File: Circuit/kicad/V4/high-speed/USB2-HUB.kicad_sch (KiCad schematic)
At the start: 37 parts, among them J10 USB_C_Receptacle_USB2.0_16P, J7 690-008-221-904, J8 USB_C_Receptacle_USB2.0_16P, U10 TPD4EUSB30, U11 USB2514B-I/M2, U12 TPD4EUSB30, U13 FSUSB42MUX, U8 FSUSB42MUX, U9 AP22653W6, Y1 24MHz

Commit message: high speed first step
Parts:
- renumbered C13 to C15, C12 to C16, C14 to C17, C17 to C18, C18 to C19, C19 to C20, C20 to C21, C21 to C22, C15 to C23, C16 to C24, CT2 to CT3, J8 to J10, J10 to J11, J7 to J12, R23 to R15, R30 to R16, R24 to R17, R32 to R18, R17 to R19, R28 to R20, R16 to R21, R27 to R22, R18 to R23, R22 to R24, R19 to R25, R20 to R26, R21 to R27, R25 to R28, R26 to R29, TP9 to TP35, U13 to U10, U9 to U13, U10 to U9
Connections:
- net CH343P_usbD+ is gone; now on net ESP_usbD+: U10.3 (D_P)
- net CH343P_usbD- is gone; now on net ESP_usbD-: U10.4 (D_N)
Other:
- moved on the sheet: C18, C19, C20, C21, C22, C23, C24, CT3, J11, J12, R16, R18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

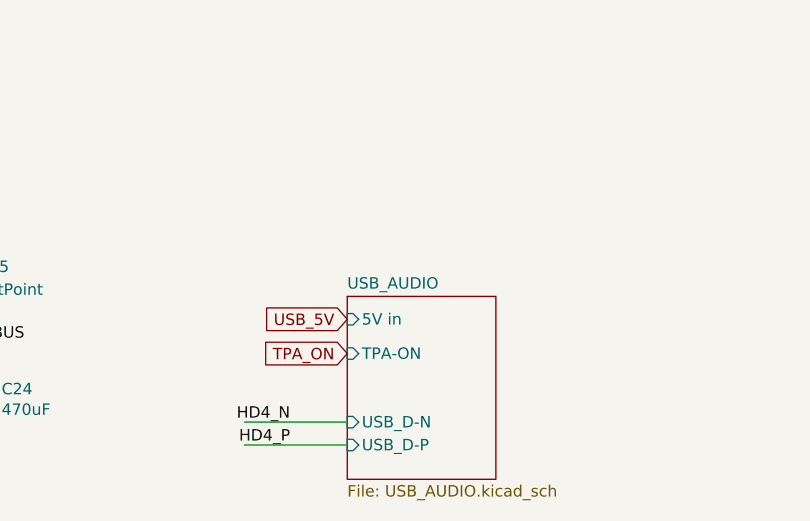
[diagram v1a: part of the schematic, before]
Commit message: added psu start delay rc tag, high speed first inner and outboard impedance calculations
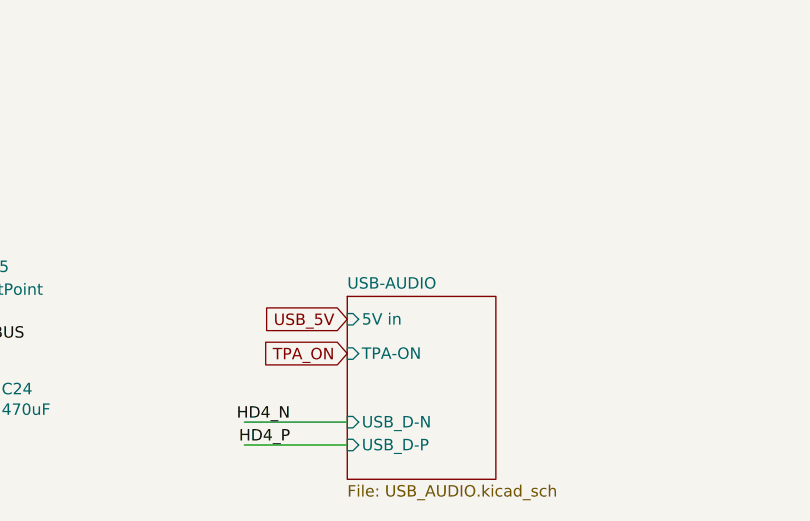
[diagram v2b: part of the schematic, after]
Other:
- sheet USB_AUDIO renamed USB-AUDIO
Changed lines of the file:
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@@
 			(color 0 0 0 0.0000)
 		)
-		(property "Sheetname" "USB_AUDIO"
+		(property "Sheetname" "USB-AUDIO"
 			(at 182.88 245.6684 0)
 			(effects

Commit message: kicad: high speed V2.2 Circuit finish psu bom update
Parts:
- C21: renamed from C15; Cikkszám (none) -> 100.011.22; Link (none) -> https://www.hestore.hu/prod_10001122.html
- C22: renamed from C16; Cikkszám (none) -> 100.011.31; Field4 Digikey -> (none); Field5 490-17672-1-ND -> (none); Field6 GJM1555C1H270JB01D -> (none); Field7 Murata -> (none); Field8 UCAP00738 -> (none); Link (none) -> https://www.hestore.hu/prod_10001131.html; Part Description 27pF 5% 50V Ceramic Capacitor C0G, NP0 0402 (1005 Metric) -> (none)
- C23: renamed from C17; Cikkszám (none) -> 100.011.31; Field4 Digikey -> (none); Field5 490-17672-1-ND -> (none); Field6 GJM1555C1H270JB01D -> (none); Field7 Murata -> (none); Field8 UCAP00738 -> (none); Link (none) -> https://www.hestore.hu/prod_10001131.html; Part Description 27pF 5% 50V Ceramic Capacitor C0G, NP0 0402 (1005 Metric) -> (none)
- C24: renamed from C18; Cikkszám (none) -> 100.277.53; Link (none) -> https://www.hestore.hu/prod_10027753.html
- C25: renamed from C19; Cikkszám (none) -> 100.277.53; Link (none) -> https://www.hestore.hu/prod_10027753.html
- C26: renamed from C20; Cikkszám (none) -> 100.277.53; Link (none) -> https://www.hestore.hu/prod_10027753.html
- C27: renamed from C21; Cikkszám (none) -> 100.277.53; Link (none) -> https://www.hestore.hu/prod_10027753.html
- C28: renamed from C22; Cikkszám (none) -> 100.277.53; Link (none) -> https://www.hestore.hu/prod_10027753.html
- C29: renamed from C23; value 10u -> 10uF; Cikkszám (none) -> 100.230.37; Field4 Digikey -> (none); Field5 490-14381-1-ND -> (none); Field6 GRM21BR71A106KA73L -> (none); Field7 Murata -> (none); Field8 111893011 -> (none); Link (none) -> https://www.hestore.hu/prod_10023037.html; Part Description 10uF 10% 10V Ceramic Capacitor X7R 0805 (2012 Metric) -> (none)
- C30: renamed from C24; Cikkszám (none) -> 100.392.15; Field4 Mouser -> (none); Field5 667-EEF-CX0J101R -> (none); Link (none) -> https://www.hestore.hu/prod_10039215.html; Part Description Capacitor, SP-Cap, 100u, 6.3V, 15mR ESR -> (none)
- CT5: renamed from CT3; value 100uf -> 100uF; Cikkszám (none) -> 100.286.19; Link (none) -> https://www.hestore.hu/prod_10028619.html
- J11: renamed from J10; Cikkszám (none) -> 100.469.70; Link (none) -> https://www.hestore.hu/prod_10046970.html
- J12: renamed from J11; Cikkszám (none) -> 100.469.70; Link (none) -> https://www.hestore.hu/prod_10046970.html
- J13: renamed from J12; footprint psu:MOLEX_USB_67298-4090 -> panel:MOLEX_USB_67298-4090; Cikkszám (none) -> 100.491.17; Field4 Farnell -> (none); Field5 2751688 -> (none); Field6 None -> (none); Field7 Molex -> (none); Field8 None -> (none); Link (none) -> https://www.hestore.hu/prod_10049117.html; Part Description USB-A (USB TYPE-A), Stacked Receptacle Connector 8 Position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 -> (none)
- R26: renamed from R15; value 5.1K 1% -> 5.1K; Cikkszám (none) -> 100.013.49; Field4 Farnell -> (none); Field5 9239278 -> (none); Field6 RK73G1ETQTP2201D -> (none); Field7 KOA EUROPE GMBH -> (none); Field8 120889581 -> (none); Link (none) -> https://www.hestore.hu/prod_10001349.html; Part Description Resistor 2.2K M1005 1% 63mW -> (none)
- R27: renamed from R16; value 5.1K 1% -> 5.1K; Cikkszám (none) -> 100.013.49; Field4 Farnell -> (none); Field5 9239278 -> (none); Field6 RK73G1ETQTP2201D -> (none); Field7 KOA EUROPE GMBH -> (none); Field8 120889581 -> (none); Link (none) -> https://www.hestore.hu/prod_10001349.html; Part Description Resistor 2.2K M1005 1% 63mW -> (none)
- R28: renamed from R17; value 5.1K 1% -> 5.1K; Cikkszám (none) -> 100.013.49; Field4 Farnell -> (none); Field5 9239278 -> (none); Field6 RK73G1ETQTP2201D -> (none); Field7 KOA EUROPE GMBH -> (none); Field8 120889581 -> (none); Link (none) -> https://www.hestore.hu/prod_10001349.html; Part Description Resistor 2.2K M1005 1% 63mW -> (none)
- R29: renamed from R18; value 5.1K 1% -> 5.1K; Cikkszám (none) -> 100.013.49; Field4 Farnell -> (none); Field5 9239278 -> (none); Field6 RK73G1ETQTP2201D -> (none); Field7 KOA EUROPE GMBH -> (none); Field8 120889581 -> (none); Link (none) -> https://www.hestore.hu/prod_10001349.html; Part Description Resistor 2.2K M1005 1% 63mW -> (none)
- R30: renamed from R19; value 2.2K 1% -> 2.2K; Cikkszám (none) -> 100.406.77; Field4 Farnell -> (none); Field5 9239278 -> (none); Field6 RK73G1ETQTP2201D -> (none); Field7 KOA EUROPE GMBH -> (none); Field8 120889581 -> (none); Link (none) -> https://www.hestore.hu/prod_10040677.html; Part Description Resistor 2.2K M1005 1% 63mW -> (none)
- R31: renamed from R20; value 2.2K 1% -> 2.2K; Cikkszám (none) -> 100.406.77; Field4 Farnell -> (none); Field5 9239278 -> (none); Field6 RK73G1ETQTP2201D -> (none); Field7 KOA EUROPE GMBH -> (none); Field8 120889581 -> (none); Link (none) -> https://www.hestore.hu/prod_10040677.html; Part Description Resistor 2.2K M1005 1% 63mW -> (none)
- R32: renamed from R21; value 2.2K 1% -> 10K; Cikkszám (none) -> 100.011.45; Field4 Farnell -> (none); Field5 9239278 -> (none); Field6 RK73G1ETQTP2201D -> (none); Field7 KOA EUROPE GMBH -> (none); Field8 120889581 -> (none); Link (none) -> https://www.hestore.hu/prod_10001145.html; Part Description Resistor 2.2K M1005 1% 63mW -> (none)
- R33: renamed from R22; value 2.2K 1% -> 10K; Cikkszám (none) -> 100.011.45; Field4 Farnell -> (none); Field5 9239278 -> (none); Field6 RK73G1ETQTP2201D -> (none); Field7 KOA EUROPE GMBH -> (none); Field8 120889581 -> (none); Link (none) -> https://www.hestore.hu/prod_10001145.html; Part Description Resistor 2.2K M1005 1% 63mW -> (none)
- R34: renamed from R23; value 10k -> 10K; Cikkszám (none) -> 100.011.45; Link (none) -> https://www.hestore.hu/prod_10001145.html
- R35: renamed from R24; value 12K 1% -> 12K; Cikkszám (none) -> 100.011.48; Field4 Farnell -> (none); Field5 9239367 -> (none); Field6 MCR01MZPF1202 -> (none); Field7 Rohm -> (none); Link (none) -> https://www.hestore.hu/prod_10001148.html; Part Description Resistor 12K M1005 1% 63mW -> (none)
- R36: renamed from R25; value 36K 1% -> 36K; Cikkszám (none) -> 100.491.04; Field4 Farnell -> (none); Field5 1458788 -> (none); Field6 MCR01MZPF3602 -> (none); Field7 Rohm -> (none); Link (none) -> https://www.hestore.hu/prod_10049104.html; Part Description Resistor 36K M1005 1% 63mW -> (none)
- R37: renamed from R26; value 36K 1% -> 36K; Cikkszám (none) -> 100.491.04; Field4 Farnell -> (none); Field5 1458788 -> (none); Field6 MCR01MZPF3602 -> (none); Field7 Rohm -> (none); Link (none) -> https://www.hestore.hu/prod_10049104.html; Part Description Resistor 36K M1005 1% 63mW -> (none)
- R38: renamed from R27; value 36K 1% -> 36K; Cikkszám (none) -> 100.491.04; Field4 Farnell -> (none); Field5 1458788 -> (none); Field6 MCR01MZPF3602 -> (none); Field7 Rohm -> (none); Link (none) -> https://www.hestore.hu/prod_10049104.html; Part Description Resistor 36K M1005 1% 63mW -> (none)
- R39: renamed from R28; value 36K 1% -> 36K; Cikkszám (none) -> 100.491.04; Field4 Farnell -> (none); Field5 1458788 -> (none); Field6 MCR01MZPF3602 -> (none); Field7 Rohm -> (none); Link (none) -> https://www.hestore.hu/prod_10049104.html; Part Description Resistor 36K M1005 1% 63mW -> (none)
- R40: renamed from R29; value 15K 1% -> 15K; Cikkszám (none) -> 100.437.82; Field4 Farnell -> (none); Field5 9239375 -> (none); Field6 MCR01MZPF1502 -> (none); Field7 Rohm -> (none); Field8 120891581 -> (none); Link (none) -> https://www.hestore.hu/prod_10043782.html; Part Description Resistor 15K M1005 1% 63mW -> (none)
- TP8: renamed from TP35; Cikkszám (none) -> -; Link (none) -> -; now left out of the parts list
- U10, U8: Cikkszám (none) -> 100.491.19; Field4 Farnell -> (none); Field5 2564479 -> (none); Field6 FSUSB42MUX -> (none); Field7 Onsemi -> (none); Link (none) -> https://www.hestore.hu/prod_10049119.html; Part Description USB Switch IC 1 Channel 10-MSOP -> (none)
- U11: Cikkszám (none) -> 100.491.01; Field4 Farnell -> (none); Field5 2775060 -> (none); Field6 USB2514B-I/M2 -> (none); Field7 Microchip -> (none); Field8 UICC00931 -> (none); Link (none) -> https://www.hestore.hu/prod_10049101.html; Part Description USB Hub Controller USB Interface 36-SQFN (6x6) -> (none)
- U12, U9: Cikkszám (none) -> 100.490.99; Field4 Farnell -> (none); Field5 2335455 -> (none); Field6 CDDFN10-3324P-13 -> (none); Field7 Bourns -> (none); Field8 UDIO00346 -> (none); Link (none) -> https://www.hestore.hu/prod_10049099.html; Part Description Quad TVS diode for high speed signals (USB3, GigE etc.) -> (none)
- U13: Cikkszám (none) -> 100.460.82; Field4 Digikey -> (none); Field5 AP2553W6-7DICT-ND -> (none); Field6 AP22653W6 -> (none); Field7 Diodes -> (none); Link (none) -> https://www.hestore.hu/prod_10046082.html; Part Description Power Switch/Driver 1:1 P-Channel 2.1A SOT-23-6 -> (none)
- Y1: Cikkszám (none) -> 100.370.19; Field4 Farnell -> (none); Field5 2508493 -> (none); Field6 X24M000000S128 -> (none); Field7 AEL -> (none); Link (none) -> https://www.hestore.hu/prod_10037019.html; Part Description 24MHz Crystal 18pf 30ppm 30ppm -> (none)
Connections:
- net GND: now also U12.3 (GND), U12.8 (GND)
- net USBF_N: now reaches J12.A7 (D-), J12.B7 (D-), U10.8 (HSD1_M)
- net USBF_N: now also U9.5 (D2-), U9.6
- net USBF_P: now reaches J12.A6 (D+), J12.B6 (D+), U10.9 (HSD1_P)
- net USBF_P: now also U9.4 (D2+), U9.7
- no-connect marks 12 -> 10
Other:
- sheet USB-AUDIO ports: added none; removed TPA-ON
- moved on the sheet: C30, R31, R33, U10, U9

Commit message: finished high-speed panel schematic and first try to doute gpios
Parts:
- removed C24, C25, C26: 1uf, Capacitor_SMD:C_0805_2012Metric, symbol Device:C
- removed C30: 470uF, Capacitor_SMD:CP_Elec_8x10, symbol Device:CP
- removed U12: TPD4EUSB30, Package_SON:USON-10_2.5x1.0mm_P0.5mm, symbol CM4IO:TPD4EUSB30
- added CT10: 100uF, Capacitor_Tantalum_SMD:CP_EIA-3528-21_Kemet-B, symbol Device:C_Polarized_Small
- C27: value 1uf -> 100nf
- C29: footprint Capacitor_Tantalum_SMD:CP_EIA-3528-21_Kemet-B -> Capacitor_Tantalum_SMD:CP_EIA-3216-18_Kemet-A_HandSolder
- CT5: footprint Capacitor_Tantalum_SMD:CP_EIA-7343-31_Kemet-D -> Capacitor_Tantalum_SMD:CP_EIA-3528-21_Kemet-B
- J11: value USB_C_Receptacle_USB2.0_16P -> USB_C_FLASH-RPI
- J12: value USB_C_Receptacle_USB2.0_16P -> USB_C_ESP
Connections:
- net +3.3v: no longer C27.1, C28.1, CT5.1, U11.10 (VDDA33), U11.15 (VDD33), U11.23 (VDD33), U11.27 (VBUS_DET), U11.29 (VDDA33), U11.36 (VDDA33), U11.5 (VDDA33)
- net GND: now also C22.1, C23.1, CT10.2; no longer C22.2, C23.2
- net USBD_N: now also J11.A7 (D-), J11.B7 (D-), U9.1 (D1+), U9.10; no longer J11.A6 (D+), J11.B6 (D+), U9.2 (D1-), U9.9
- net USBD_P: now also J11.A6 (D+), J11.B6 (D+), U9.2 (D1-), U9.9; no longer J11.A7 (D-), J11.B7 (D-), U9.1 (D1+), U9.10
- net USBF_N: now also U9.4 (D2+), U9.7; no longer U9.5 (D2-), U9.6
- net USBF_P: now also U9.5 (D2-), U9.6; no longer U9.4 (D2+), U9.7
- net VBUS: now also CT10.1
- net USB_5V renamed USB_5v
- new net: C23.2, U11.32 (XTALOUT), Y1.1
- new net: C22.2, U11.33 (XTALIN/CLKIN), Y1.2
- new net ESP_3v3: C27.1, C28.1, CT5.1, U11.10 (VDDA33), U11.15 (VDD33), U11.23 (VDD33), U11.27 (VBUS_DET), U11.29 (VDDA33), U11.36 (VDDA33), U11.5 (VDDA33)
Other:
- note added: "ESP JTAG & programming"
- note added: "RPI EMMC flash"
- note added: "USB current limit switch for connectors"
- note removed: "Current Limit switch"
- moved on the sheet: C21, C22, C23, C27, C28, C29, CT5, J11, J12, J13, R26, R27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

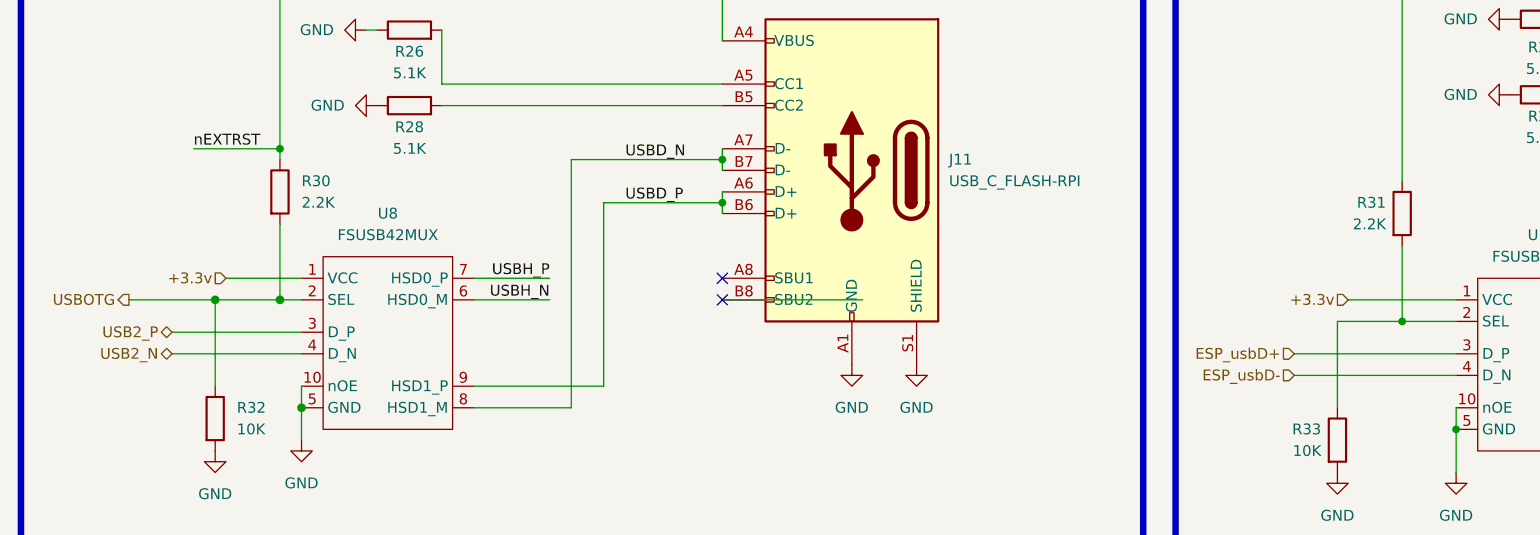
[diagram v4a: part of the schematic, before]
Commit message: High Speed all routed, DRC, DFM shows 0 error (without silkscreen layers)
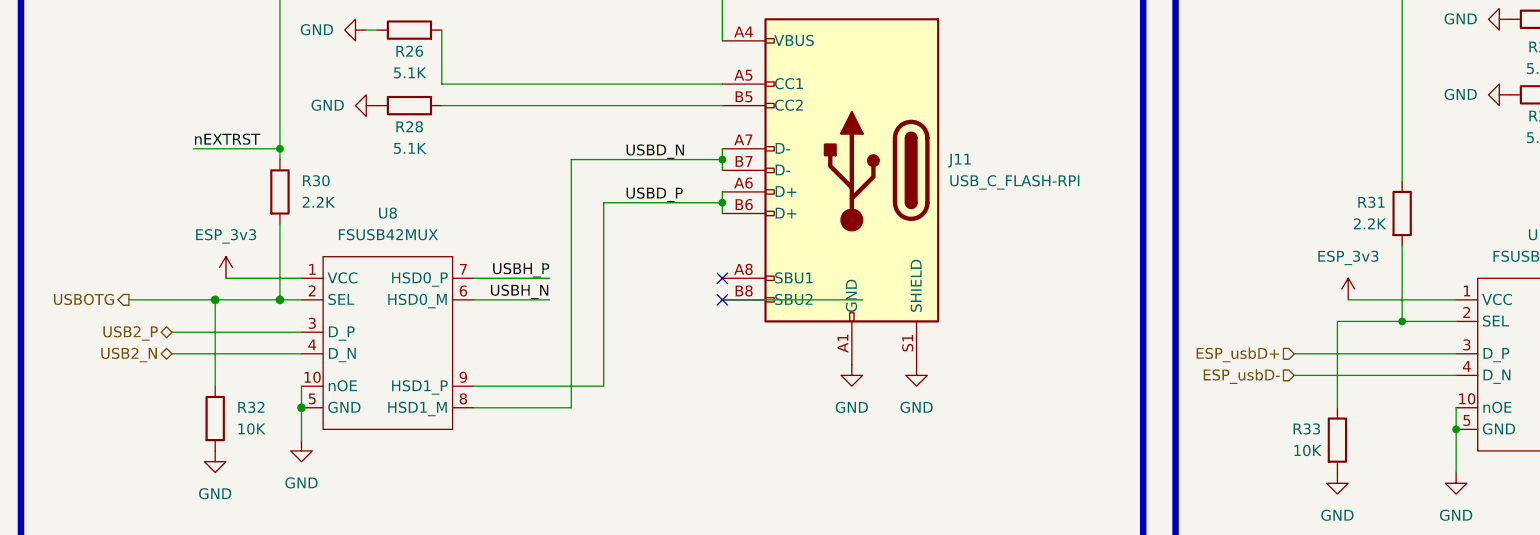
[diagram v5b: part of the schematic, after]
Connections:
- net +3.3v is gone; now on net ESP_3v3: U10.1 (VCC), U8.1 (VCC)
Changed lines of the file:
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@@
 		)
 	)
-	(hierarchical_label "+3.3v"
-		(shape input)
-		(at 40.64 63.5 180)
-		(effects
-			(font
-				(size 1.27 1.27)
-			)
-			(justify right)
-		)
-	)
 	(hierarchical_label "ESP_usbD+"
 		(shape input)
@@
 		)
 	)
-	(hierarchical_label "+3.3v"
-		(shape input)
-		(at 172.72 66.04 180)
-		(effects
-			(font
-				(size 1.27 1.27)
-			)
-			(justify right)
-		)
-	)
 	(symbol
 		(lib_id "CM4IO:USB_67298-4090")
@@
 	)
 	(symbol
+		(lib_id "power:+1V0")
+		(at 172.72 66.04 0)
+		(unit 1)
+		(exclude_from_sim no)
+		(in_bom yes)
+		(on_board yes)
+		(dnp no)
+		(fields_autoplaced yes)
+		(property "Reference" "#PWR0220"
+			(at 172.72 69.85 0)
+			(effects
+				(font
+					(size 1.27 1.27)
+				)
+				(hide yes)
+			)
+		)
+		(property "Value" "ESP_3v3"
+			(at 172.72 60.96 0)
+			(effects
+				(font
+					(size 1.27 1.27)
+				)
+			)
+		)
+		(property "Footprint" ""
+			(at 172.72 66.04 0)
+			(effects
+				(font
+					(size 1.27 1.27)
+				)
+				(hide yes)
+			)
+		)
+		(property "Datasheet" ""
+			(at 172.72 66.04 0)
+			(effects
+				(font
+					(size 1.27 1.27)
+				)
+				(hide yes)
+			)
+		)
+		(property "Description" "Power symbol creates a global label with name \"+1V0\""
+			(at 172.72 66.04 0)
+			(effects
+				(font
+					(size 1.27 1.27)
+				)
+				(hide yes)
+			)
+		)
+		(pin "1"
+		)
+		(instances
+			(project "high-speed"
+				(path "/e63e39d7-6ac0-4ffd-8aa3-1841a4541b55/cff930b7-73aa-4016-850e-19e704dc474e"
+					(reference "#PWR0220")
+					(unit 1)
+				)
+			)
+		)
+	)
+	(symbol
 		(lib_id "Device:C_Polarized_Small")
 		(at 227.33 153.67 0)
@@
 					(unit 1)
 				)
+			)
+		)
+	)
+	(symbol
+		(lib_id "power:+1V0")
+		(at 40.64 63.5 0)
+		(unit 1)
+		(exclude_from_sim no)
+		(in_bom yes)
+		(on_board yes)
+		(dnp no)
+		(fields_autoplaced yes)
+		(property "Reference" "#PWR0158"
+			(at 40.64 67.31 0)
+			(effects
+				(font
+					(size 1.27 1.27)
+				)
+				(hide yes)
+			)
+		)
+		(property "Value" "ESP_3v3"
+			(at 40.64 58.42 0)
+			(effects
+				(font
+					(size 1.27 1.27)
+				)
+			)
+		)
+		(property "Footprint" ""
+			(at 40.64 63.5 0)
+			(effects
+				(font
+					(size 1.27 1.27)
+				)
+				(hide yes)
+			)
+		)
+		(property "Datasheet" ""
+			(at 40.64 63.5 0)
+			(effects
+				(font
+					(size 1.27 1.27)
+				)
+				(hide yes)
+			)
+		)
+		(property "Description" "Power symbol creates a global label with name \"+1V0\""
+			(at 40.64 63.5 0)
+			(effects
+				(font
+					(size 1.27 1.27)
+				)
+				(hide yes)
+			)
+		)
+		(pin "1"
+		)
+		(instances
+			(project "high-speed"
+				(path "/e63e39d7-6ac0-4ffd-8aa3-1841a4541b55/cff930b7-73aa-4016-850e-19e704dc474e"
+					(reference "#PWR0158")
+					(unit 1)
+				)
